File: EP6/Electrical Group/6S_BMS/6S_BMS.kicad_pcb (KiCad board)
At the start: 4 copper layers, 100 x 70 mm, 188 parts, among them J1 battery cells, J10 I2C1, J11 CAN1, J12 frontBox, J13 USB_C_stm32, J2 GLVMS, J3 BOOT_BTN, J4 24Vout, J5 CHARGE, J6 UART2, J7 SWD, J8 7seg, J9 RESET, Q1 HSBA3119, Q10 SI2301CDS-T1-GE3, Q11 SI2301CDS-T1-GE3, Q12 SI2301CDS-T1-GE3, Q13 SI2301CDS-T1-GE3, Q14 SI2301CDS-T1-GE3, Q15 SI2301CDS-T1-GE3, Q2 2N7002, Q3 2N7002, Q4 HSBA3119, Q5 2N7002, Q6 2N7002, Q7 AO3401A, Q9 HSBA3119, SW1 RESET, U1 78L05G-AB3-R, U2 HT7533, U3 BQ7693003, U4 TCAN1042VDRQ1, U5 STM32F103C8Tx, U6 CAT24C256, U7 LM66100DCK, U8 LM74700, Y1 8MHz X49SM8MSD2SC

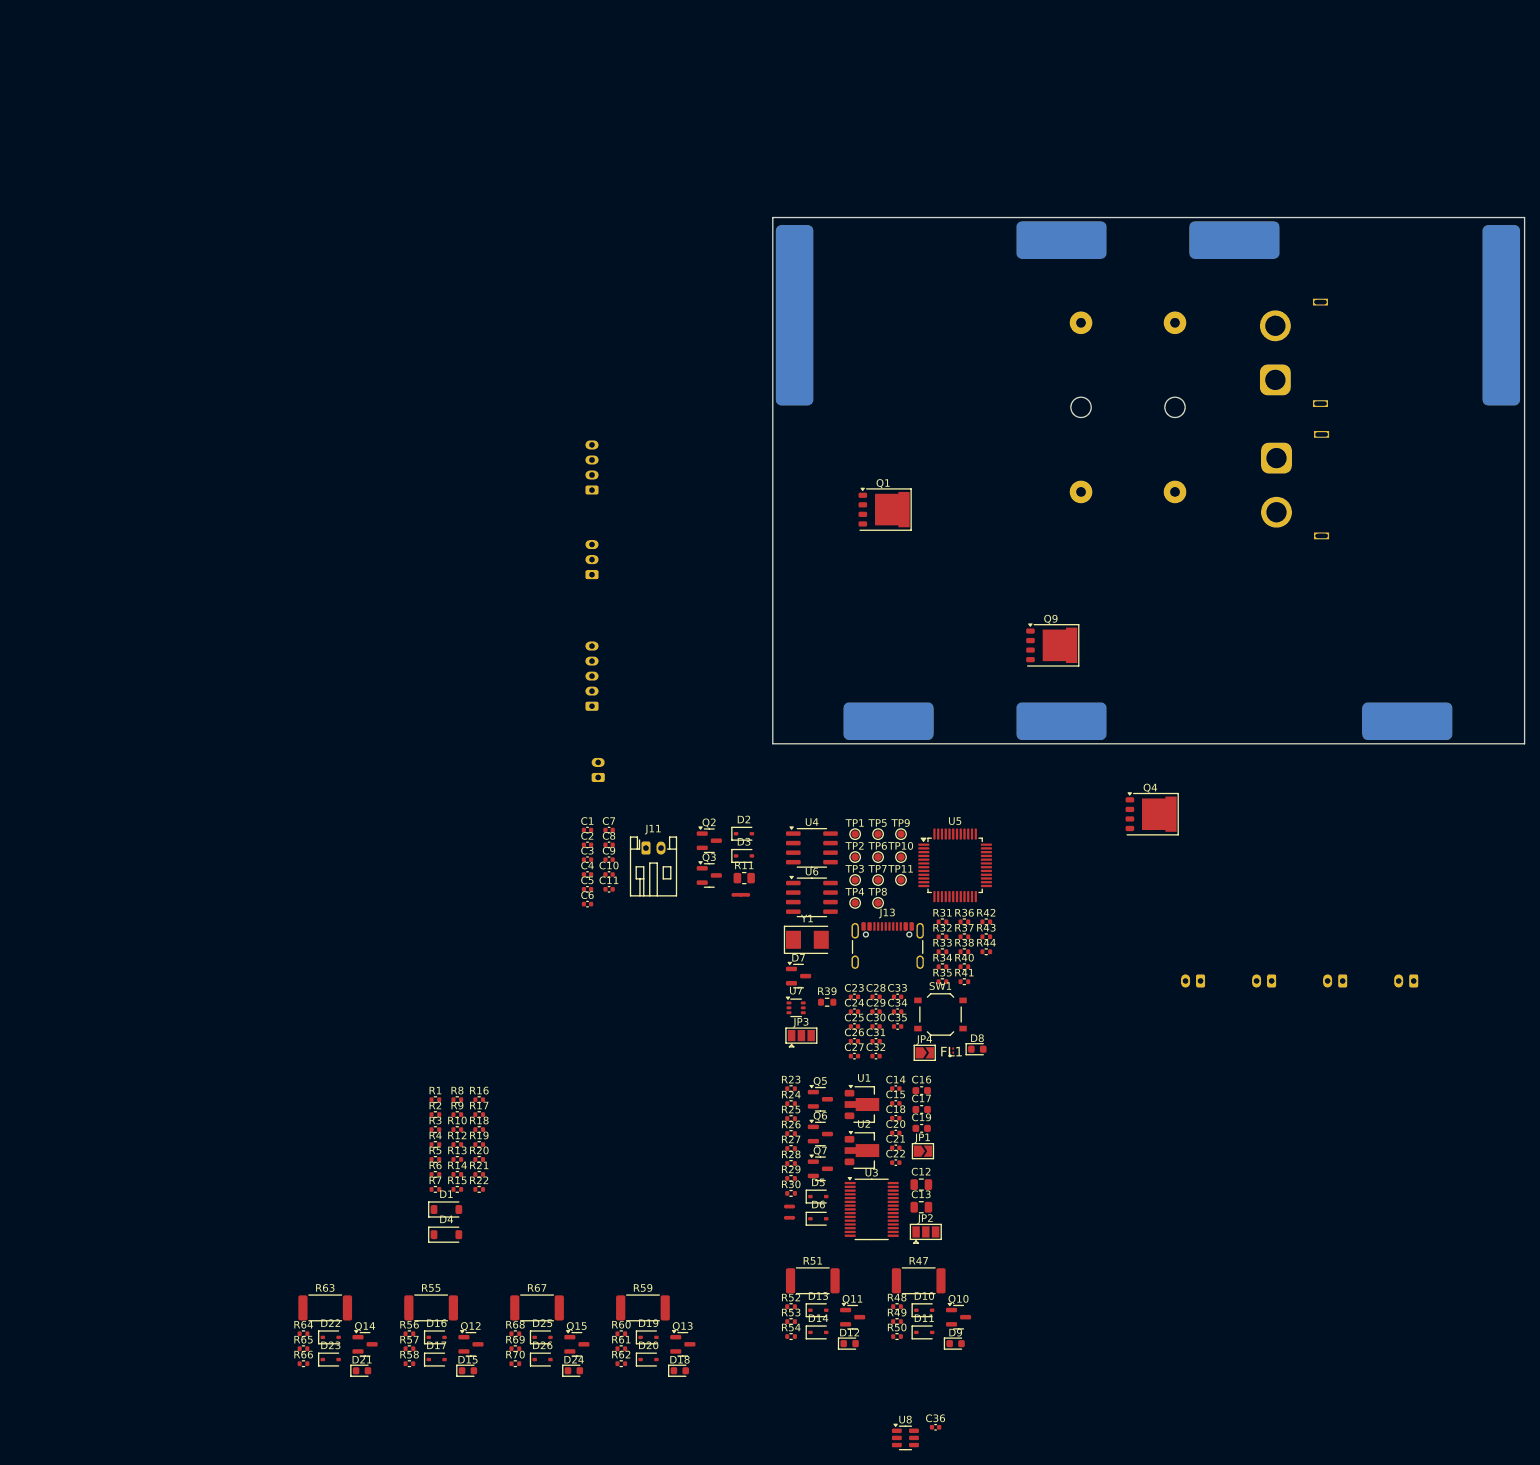
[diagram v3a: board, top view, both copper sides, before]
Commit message: front panel board connectors
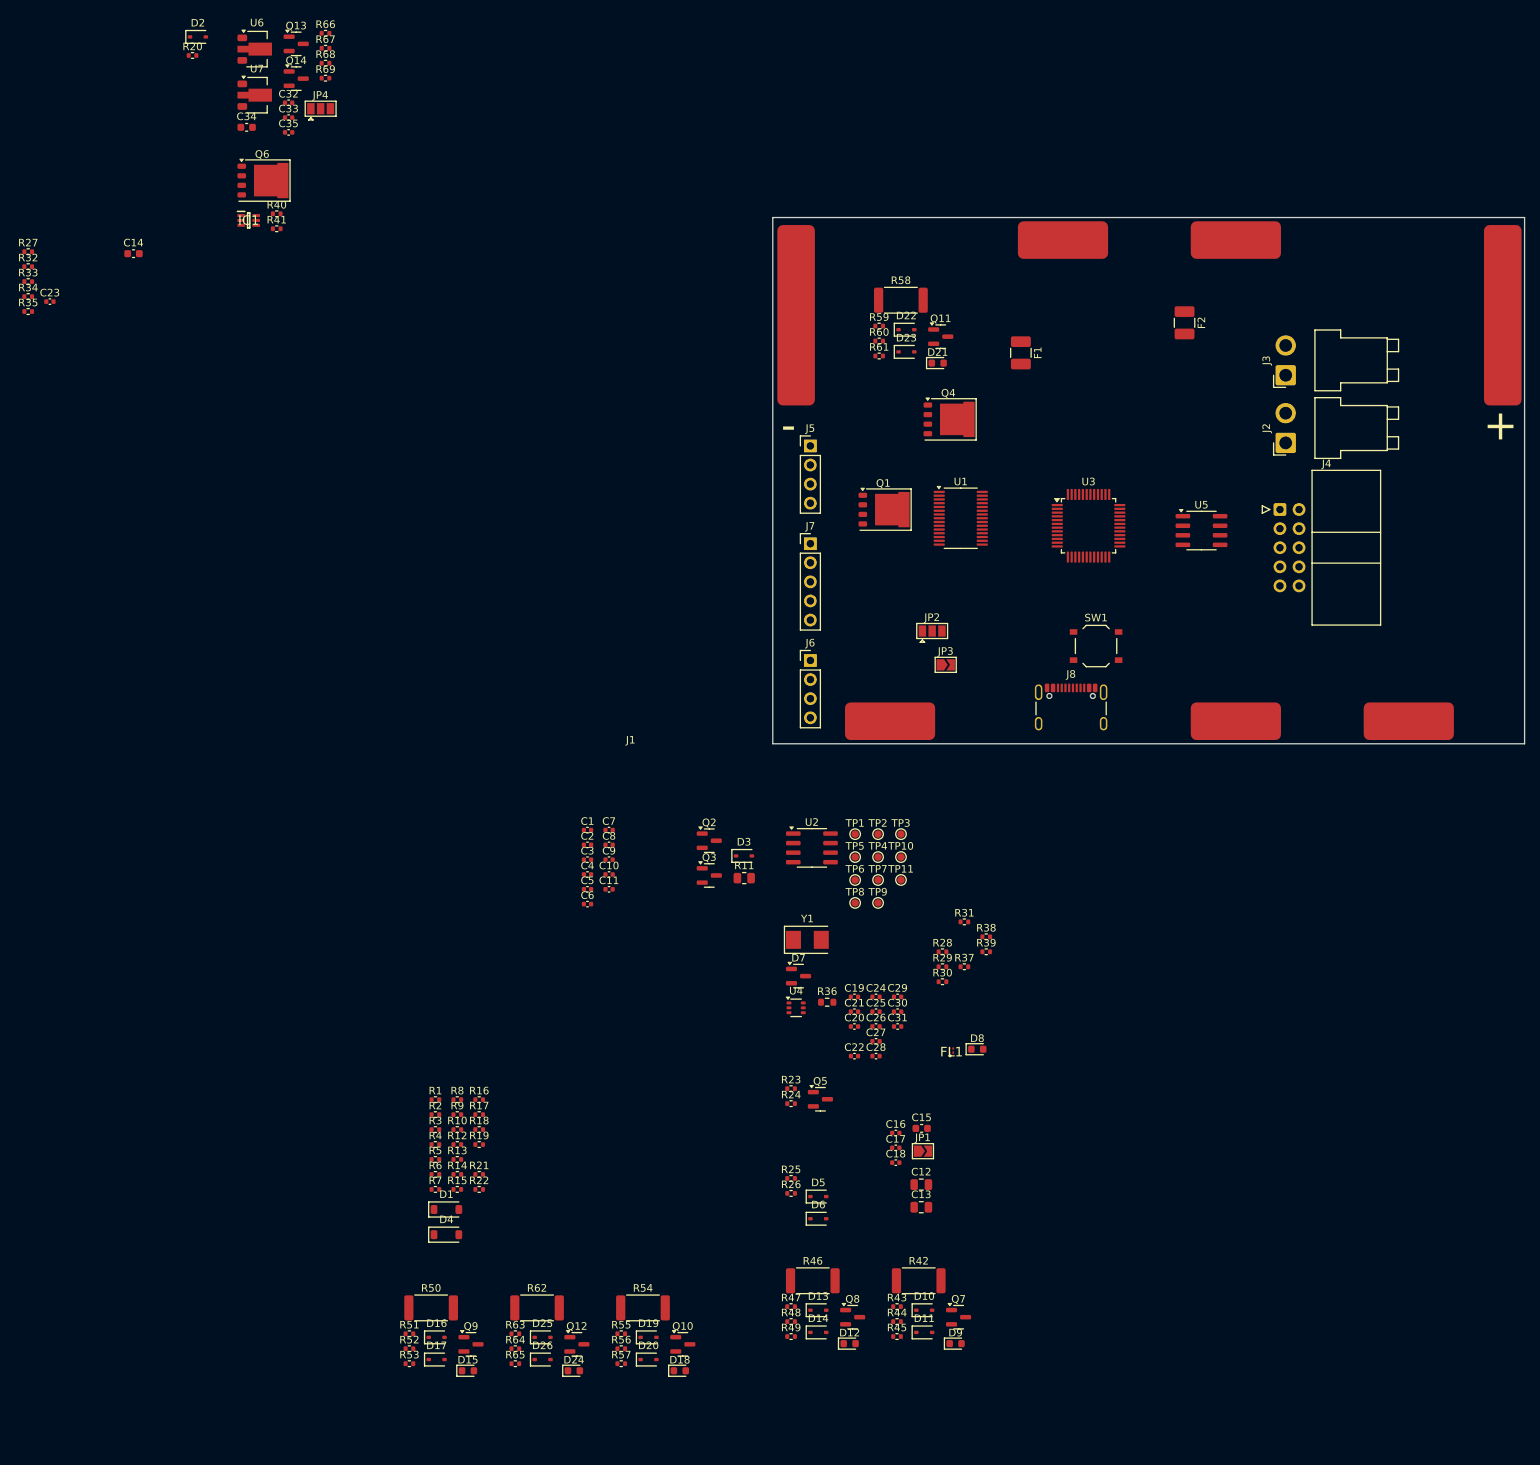
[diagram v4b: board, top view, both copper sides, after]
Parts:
- removed the C15 at (116.4, 142.8)
- removed the C16 at (119.8, 141.1)
- removed the C17 at (119.8, 143.6)
- removed the C18 at (116.4, 144.8)
- removed the C26 at (110.9, 134.6)
- removed C36: 220nF 25V, Capacitor_SMD:C_0402_1005Metric
- removed J10: I2C1, Connector_JST:JST_PH_S2B-PH-K_1x02_P2.00mm_Horizontal
- removed J11: CAN1, Connector_JST:JST_PH_S2B-PH-K_1x02_P2.00mm_Horizontal
- removed J12: frontBox, Connector_JST:JST_PH_S4B-PH-K_1x04_P2.00mm_Horizontal
- removed the J2 at (76.8, 99.5)
- removed the J3 at (185.2, 126.5)
- removed the J8 at (76.0, 90.0)
- removed J9: RESET, Connector_JST:JST_PH_S2B-PH-K_1x02_P2.00mm_Horizontal
- removed the JP2 at (120.4, 159.9)
- removed NT1: CELL_NEG_TIE, NetTie:NetTie-3_SMD_Pad0.5mm
- removed NT2, NT3: NetTie_2, NetTie:NetTie-2_SMD_Pad0.5mm
- removed the Q7 at (106.3, 151.5)
- removed the Q9 at (137.0, 81.9)
- removed the R25 at (102.4, 144.9)
- removed the R26 at (102.4, 146.8)
- removed the R28 at (102.4, 150.8)
- removed the R31 at (122.6, 118.7)
- removed the R37 at (125.5, 120.7)
- removed the R38 at (125.5, 122.7)
- removed the R42 at (128.4, 118.7)
- removed the U1 at (112.2, 143.0)
- removed the U2 at (112.2, 149.1)
- removed U8: LM74700, Package_TO_SOT_SMD:SOT-23-6
- added C23: 0u1, Capacitor_SMD:C_0402_1005Metric, F.Cu at (3.85, 36.2)
- added C32: 1u, Capacitor_SMD:C_0402_1005Metric, F.Cu at (35.6, 9.73)
- added C33: 1u, Capacitor_SMD:C_0402_1005Metric, F.Cu at (35.6, 11.7)
- added C34: 10u, Capacitor_SMD:C_0603_1608Metric, F.Cu at (30.0, 13.0)
- added C35: 10u, Capacitor_SMD:C_0402_1005Metric, F.Cu at (35.6, 13.7)
- added IC1: DZDH0401DW-7, SamacSys_Parts_EP6:SOT65P210X110-6N, F.Cu at (30.3, 25.4)
- added J4: HVB_Front_Panel, Connector_IDC:IDC-Header_2x05_P2.54mm_Horizontal, F.Cu at (167.5, 63.8)
- added J5: UART, Connector_PinHeader_2.54mm:PinHeader_1x04_P2.54mm_Vertical, F.Cu at (105.0, 55.4)
- added JP4: 3V3 select, Jumper:SolderJumper-3_P1.3mm_Open_Pad1.0x1.5mm, F.Cu at (39.9, 10.5)
- added Q13: 2N7002, Package_TO_SOT_SMD:SOT-23, F.Cu at (36.6, 1.90)
- added Q14: AO3401A, Package_TO_SOT_SMD:SOT-23, F.Cu at (36.6, 6.53)
- added R33: 4k7, Resistor_SMD:R_0402_1005Metric, F.Cu at (0.95, 33.5)
- added R34: 10R, Resistor_SMD:R_0402_1005Metric, F.Cu at (0.95, 35.5)
- added R35: 10R, Resistor_SMD:R_0402_1005Metric, F.Cu at (0.95, 37.5)
- added R40: Rref, Resistor_SMD:R_0402_1005Metric, F.Cu at (34.0, 24.5)
- added R66: 1k, Resistor_SMD:R_0402_1005Metric, F.Cu at (40.5, 0.49)
- added R67: 1M, Resistor_SMD:R_0402_1005Metric, F.Cu at (40.5, 2.48)
- added R68: 470k, Resistor_SMD:R_0402_1005Metric, F.Cu at (40.5, 4.47)
- added R69: 1M, Resistor_SMD:R_0402_1005Metric, F.Cu at (40.5, 6.46)
- added U6: 78L05G-AB3-R, Package_TO_SOT_SMD:SOT-89-3, F.Cu at (31.4, 2.60)
- added U7: HT7533, Package_TO_SOT_SMD:SOT-89-3, F.Cu at (31.4, 8.72)
- C14: value 1u -> 4u7 16V; footprint Capacitor_SMD:C_0402_1005Metric -> Capacitor_SMD:C_0603_1608Metric
- F1: footprint Fuse:Fuseholder_Cylinder-5x20mm_Schurter_0031_8201_Horizontal_Open -> Fuse:Fuse_1210_3225Metric_Pad1.42x2.65mm_HandSolder; moved to F.Cu
- F2: value 10A ext fuse -> 10A EXT fuse; footprint Fuse:Fuseholder_Cylinder-5x20mm_Schurter_0031_8201_Horizontal_Open -> Fuse:Fuse_1210_3225Metric_Pad1.42x2.65mm_HandSolder; moved to F.Cu
- J1: value battery cells -> Cell Pads; moved to F.Cu
- J2: renamed from J4; value 24Vout -> 24V_OUT; footprint Connector_AMASS:AMASS_XT60PW-F_1x02_P7.20mm_Horizontal -> Connector_JST:JST_VH_B2PS-VH_1x02_P3.96mm_Horizontal; moved to F.Cu
- J3: renamed from J5; footprint Connector_AMASS:AMASS_XT60PW-M_1x02_P7.20mm_Horizontal -> Connector_JST:JST_VH_B2PS-VH_1x02_P3.96mm_Horizontal; moved to F.Cu
- J6: value UART2 -> I2C; footprint Connector_JST:JST_PH_S2B-PH-K_1x02_P2.00mm_Horizontal -> Connector_PinHeader_2.54mm:PinHeader_1x04_P2.54mm_Vertical; moved to F.Cu
- J7: footprint Connector_JST:JST_PH_S3B-PH-K_1x03_P2.00mm_Horizontal -> Connector_PinHeader_2.54mm:PinHeader_1x05_P2.54mm_Vertical; moved to F.Cu
- JP3: renamed from JP4; value Vbus -> VUSB
- Q6: value 2N7002 -> HSBA3119; footprint Package_TO_SOT_SMD:SOT-23 -> nturt_kicad_lib_EP6:HSBA3119_PRPAK5X6
- R27: value 470k -> 10k
- R32: value 10k -> 4k7
- R41: value 10R -> Rbias
- moved R27 156.6 mm to (0.95, 29.5)
- moved D21 154.4 mm to (121.9, 44.4)
- moved D22 154.4 mm to (117.8, 39.9)
- moved Q11 154.4 mm to (122.3, 40.8)
- moved R58 154.4 mm to (117.0, 36.0)
- moved R59 154.4 mm to (114.1, 39.4)
- moved R61 154.4 mm to (114.1, 43.4)
- moved D23 154.4 mm to (117.8, 42.9)
- moved R60 154.4 mm to (114.1, 41.4)
- moved R20 151.7 mm to (22.8, 3.44)
- moved R32 150.8 mm to (0.95, 31.5)
- moved C14 150.4 mm to (15.0, 29.8)
- moved Q6 147.0 mm to (32.1, 20.1)
- moved J1 137.8 mm to (81.1, 95.0), turned to 0 degrees
- moved R41 135.6 mm to (34.0, 26.5)
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- renumbered C19 to C15, C20 to C16, C21 to C17, C22 to C18, C23 to C19, C25 to C20, C24 to C21, C27 to C22, C28 to C24, C29 to C25, C30 to C26, C31 to C27, C32 to C28, C33 to C29, C34 to C30, C35 to C31, J13 to J8, JP3 to JP2, Q13 to Q10, Q14 to Q11, Q15 to Q12, Q10 to Q7, Q11 to Q8, Q12 to Q9, R29 to R25, R30 to R26, R33 to R28, R34 to R29, R35 to R30, R36 to R31, R39 to R36, R40 to R37, R43 to R38, R44 to R39, R47 to R42, R48 to R43, R49 to R44, R50 to R45, R51 to R46, R52 to R47, R53 to R48, R54 to R49, R55 to R50, R56 to R51, R57 to R52, R58 to R53, R59 to R54, R60 to R55, R61 to R56, R62 to R57, R63 to R58, R64 to R59, R65 to R60, R66 to R61, R67 to R62, R68 to R63, R69 to R64, R70 to R65, TP5 to TP2, TP9 to TP3, TP6 to TP4, TP2 to TP5, TP3 to TP6, TP4 to TP8, TP8 to TP9, U3 to U1, U4 to U2, U5 to U3, U7 to U4, U6 to U5
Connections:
- net /BOOT_BTN renamed /MODE_CTL
- net /MCU/SPI2_CS renamed /DISP_CS
- net /MCU/SPI2_MOSI renamed /DISP_DIN
- net /MCU/SPI2_SCK renamed /DISP_CLK
- net /MCU/VBUS renamed VBUS
- net /MCU/led renamed /MCU/LED
- C14 pad 2: Net-(Q7-D) -> /REGOUT
- D1 pad 1: /PACK+ -> +24V
- D2 pad 2: Net-(D2-A) -> /CELLS+
- D3 pad 1: Net-(D3-K) -> /MODE_BTN_B
- J6 pad 1: /MCU/UART1_TX -> +3V3
- J6 pad 2: /MCU/UART1_RX -> GND
- J7 pad 2: /MCU/SWCLK -> +3V3
- J7 pad 3: /MCU/SWDIO -> /MCU/SWCLK
- J8 pad A6: /MCU/USB_D+ -> /MCU/USB_DP
- J8 pad A7: /MCU/USB_D- -> /MCU/USB_DN
- J8 pad B6: /MCU/USB_D+ -> /MCU/USB_DP
- J8 pad B7: /MCU/USB_D- -> /MCU/USB_DN
- Q4 pad D: /PACK+ -> +24V
- R20 pad 2: Net-(D3-K) -> /MODE_BTN_A
- R21 pad 2: Net-(D3-K) -> /MODE_BTN_B
- R27 pad 1: /CELLS+ -> +3V3
- R27 pad 2: Net-(Q7-G) -> /MCU_RST
- R32 pad 2: /SCL -> /MCU/I2C1_SCL
- R41 pad 1: /MCU/USB_DN -> Net-(IC1-BIAS)
- R41 pad 2: /MCU/USB_D- -> GND
- SW1 pad 2: /MCU/NRST -> /MCU_RST
- TP1 pad 1: /SCL -> /MCU/I2C1_SCL
- TP2 pad 1: /SDA -> /MCU/I2C1_SDA
- U1 pad 8: /AFE/REGOUT -> /REGOUT
- U3 pad 12: /MCU/UART1_TX -> /MCU/UART2_TX
- U3 pad 13: /MCU/UART1_RX -> /MCU/UART2_RX
- U3 pad 32: /MCU/USB_DN -> Net-(U3-PA11)
- U3 pad 33: /MCU/USB_DP -> Net-(U3-PA12)
- U3 pad 42: /SCL -> /MCU/I2C1_SCL
- U3 pad 43: /SDA -> /MCU/I2C1_SDA
- U3 pad 7: /MCU/NRST -> /MCU_RST
- U5 pad 5: /SDA -> /MCU/I2C1_SDA
- U5 pad 6: /SCL -> /MCU/I2C1_SCL
